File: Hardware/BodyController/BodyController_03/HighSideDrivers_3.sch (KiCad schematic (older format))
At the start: 48 parts, among them U12 BTS50202EKAXUMA2, U13 BTS50202EKAXUMA2, U14 BTS50202EKAXUMA2, U15 BTS716G, U23 tps25940-q1

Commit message: started serious layout
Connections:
- net GND: now also U15.6 (GND3/4)
- net ECU_1_ISENSE renamed ECU_1_ISENSE_AI
- net ECU_2_ISENSE renamed ECU_2_ISENSE_AI
- net IC_CONTROLLER_ISENSE renamed IC_CONTROLLER_ISENSE_AI
- net LOCK_ISENSE renamed LOCK_ISENSE_AI
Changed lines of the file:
@@
 EESchema Schematic File Version 2
-LIBS:BodyController_03-rescue
 LIBS:power
 LIBS:device
@@
 LIBS:contrib
 LIBS:valves
+LIBS:HSD
+LIBS:micros
+LIBS:ICs
+LIBS:Connectors
 LIBS:BodyController_03-cache
 EELAYER 25 0
@@
 $Descr A4 11693 8268
 encoding utf-8
-Sheet 7 11
+Sheet 7 12
 Title ""
 Date ""
@@
 $EndComp
 $Comp
-L GND #PWR098
+L GND #PWR080
 U 1 1 5991C550
 P 2900 7050
-F 0 "#PWR098" H 2900 6800 50  0001 C CNN
+F 0 "#PWR080" H 2900 6800 50  0001 C CNN
 F 1 "GND" H 2900 6900 50  0000 C CNN
 F 2 "" H 2900 7050 50  0001 C CNN
@@
 $EndComp
 $Comp
-L GND #PWR099
+L GND #PWR081
 U 1 1 5991C557
 P 2600 6850
-F 0 "#PWR099" H 2600 6600 50  0001 C CNN
+F 0 "#PWR081" H 2600 6600 50  0001 C CNN
 F 1 "GND" H 2600 6700 50  0000 C CNN
 F 2 "" H 2600 6850 50  0001 C CNN
@@
 $EndComp
 $Comp
-L GND #PWR0100
+L GND #PWR082
 U 1 1 5991C559
 P 2050 6850
-F 0 "#PWR0100" H 2050 6600 50  0001 C CNN
+F 0 "#PWR082" H 2050 6600 50  0001 C CNN
 F 1 "GND" H 2050 6700 50  0000 C CNN
 F 2 "" H 2050 6850 50  0001 C CNN
@@
 $EndComp
 $Comp
-L +12V #PWR0101
+L +12V #PWR083
 U 1 1 5991C55A
 P 4700 5600
-F 0 "#PWR0101" H 4700 5450 50  0001 C CNN
+F 0 "#PWR083" H 4700 5450 50  0001 C CNN
 F 1 "+12V" H 4700 5740 50  0000 C CNN
 F 2 "" H 4700 5600 50  0001 C CNN
@@
 $EndComp
 $Comp
-L +12V #PWR0102
+L +12V #PWR084
 U 1 1 5991C55C
 P 7600 750
-F 0 "#PWR0102" H 7600 600 50  0001 C CNN
+F 0 "#PWR084" H 7600 600 50  0001 C CNN
 F 1 "+12V" H 7600 890 50  0000 C CNN
 F 2 "" H 7600 750 50  0001 C CNN
@@
 $EndComp
 $Comp
-L GND #PWR0103
+L GND #PWR085
 U 1 1 5991C55D
 P 7600 2200
-F 0 "#PWR0103" H 7600 1950 50  0001 C CNN
+F 0 "#PWR085" H 7600 1950 50  0001 C CNN
 F 1 "GND" H 7600 2050 50  0000 C CNN
 F 2 "" H 7600 2200 50  0001 C CNN
@@
 $EndComp
 $Comp
-L GND #PWR0104
+L GND #PWR086
 U 1 1 5991C565
 P 2900 4900
-F 0 "#PWR0104" H 2900 4650 50  0001 C CNN
+F 0 "#PWR086" H 2900 4650 50  0001 C CNN
 F 1 "GND" H 2900 4750 50  0000 C CNN
 F 2 "" H 2900 4900 50  0001 C CNN
@@
 $EndComp
 $Comp
-L GND #PWR0105
+L GND #PWR087
 U 1 1 5991C56C
 P 2600 4700
-F 0 "#PWR0105" H 2600 4450 50  0001 C CNN
+F 0 "#PWR087" H 2600 4450 50  0001 C CNN
 F 1 "GND" H 2600 4550 50  0000 C CNN
 F 2 "" H 2600 4700 50  0001 C CNN
@@
 $EndComp
 $Comp
-L GND #PWR0106
+L GND #PWR088
 U 1 1 5991C56E
 P 2050 4700
-F 0 "#PWR0106" H 2050 4450 50  0001 C CNN
+F 0 "#PWR088" H 2050 4450 50  0001 C CNN
 F 1 "GND" H 2050 4550 50  0000 C CNN
 F 2 "" H 2050 4700 50  0001 C CNN
@@
 $EndComp
 $Comp
-L +12V #PWR0107
+L +12V #PWR089
 U 1 1 5991C56F
 P 4700 3450
-F 0 "#PWR0107" H 4700 3300 50  0001 C CNN
+F 0 "#PWR089" H 4700 3300 50  0001 C CNN
 F 1 "+12V" H 4700 3590 50  0000 C CNN
 F 2 "" H 4700 3450 50  0001 C CNN
@@
 $EndComp
 $Comp
-L GND #PWR0108
+L GND #PWR090
 U 1 1 5991C571
 P 2900 2900
-F 0 "#PWR0108" H 2900 2650 50  0001 C CNN
+F 0 "#PWR090" H 2900 2650 50  0001 C CNN
 F 1 "GND" H 2900 2750 50  0000 C CNN
 F 2 "" H 2900 2900 50  0001 C CNN
@@
 $EndComp
 $Comp
-L GND #PWR0109
+L GND #PWR091
 U 1 1 5991C578
 P 2600 2700
-F 0 "#PWR0109" H 2600 2450 50  0001 C CNN
+F 0 "#PWR091" H 2600 2450 50  0001 C CNN
 F 1 "GND" H 2600 2550 50  0000 C CNN
 F 2 "" H 2600 2700 50  0001 C CNN
@@
 $EndComp
 $Comp
-L GND #PWR0110
+L GND #PWR092
 U 1 1 5991C57A
 P 2050 2700
-F 0 "#PWR0110" H 2050 2450 50  0001 C CNN
+F 0 "#PWR092" H 2050 2450 50  0001 C CNN
 F 1 "GND" H 2050 2550 50  0000 C CNN
 F 2 "" H 2050 2700 50  0001 C CNN
@@
 $EndComp
 $Comp
-L +12V #PWR0111
+L +12V #PWR093
 U 1 1 5991C57B
 P 4700 1450
-F 0 "#PWR0111" H 4700 1300 50  0001 C CNN
+F 0 "#PWR093" H 4700 1300 50  0001 C CNN
 F 1 "+12V" H 4700 1590 50  0000 C CNN
 F 2 "" H 4700 1450 50  0001 C CNN
@@
 $EndComp
 $Comp
-L GND #PWR0112
+L GND #PWR094
 U 1 1 5991EDF3
 P 4500 7150
-F 0 "#PWR0112" H 4500 6900 50  0001 C CNN
+F 0 "#PWR094" H 4500 6900 50  0001 C CNN
 F 1 "GND" H 4500 7000 50  0000 C CNN
 F 2 "" H 4500 7150 50  0001 C CNN
@@
 $EndComp
 $Comp
-L GND #PWR0113
+L GND #PWR095
 U 1 1 5991EE88
 P 4750 7150
-F 0 "#PWR0113" H 4750 6900 50  0001 C CNN
+F 0 "#PWR095" H 4750 6900 50  0001 C CNN
 F 1 "GND" H 4750 7000 50  0000 C CNN
 F 2 "" H 4750 7150 50  0001 C CNN
@@
 $EndComp
 $Comp
-L GND #PWR0114
+L GND #PWR096
 U 1 1 59923191
 P 8950 1950
-F 0 "#PWR0114" H 8950 1700 50  0001 C CNN
+F 0 "#PWR096" H 8950 1700 50  0001 C CNN
 F 1 "GND" H 8950 1800 50  0000 C CNN
 F 2 "" H 8950 1950 50  0001 C CNN
@@
 $EndComp
 $Comp
-L GND #PWR0115
+L GND #PWR097
 U 1 1 5992320B
 P 9200 1950
-F 0 "#PWR0115" H 9200 1700 50  0001 C CNN
+F 0 "#PWR097" H 9200 1700 50  0001 C CNN
 F 1 "GND" H 9200 1800 50  0000 C CNN
 F 2 "" H 9200 1950 50  0001 C CNN
@@
 $EndComp
 $Comp
-L GND #PWR0116
+L GND #PWR098
 U 1 1 59923324
 P 9450 1950
-F 0 "#PWR0116" H 9450 1700 50  0001 C CNN
+F 0 "#PWR098" H 9450 1700 50  0001 C CNN
 F 1 "GND" H 9450 1800 50  0000 C CNN
 F 2 "" H 9450 1950 50  0001 C CNN
@@
 $EndComp
 $Comp
-L GND #PWR0117
+L GND #PWR099
 U 1 1 5992339E
 P 9700 1950
-F 0 "#PWR0117" H 9700 1700 50  0001 C CNN
+F 0 "#PWR099" H 9700 1700 50  0001 C CNN
 F 1 "GND" H 9700 1800 50  0000 C CNN
 F 2 "" H 9700 1950 50  0001 C CNN
@@
 $EndComp
 $Comp
-L +12V #PWR0118
+L +12V #PWR0100
 U 1 1 59A07BF7
 P 6200 3250
-F 0 "#PWR0118" H 6200 3100 50  0001 C CNN
+F 0 "#PWR0100" H 6200 3100 50  0001 C CNN
 F 1 "+12V" H 6200 3390 50  0000 C CNN
 F 2 "" H 6200 3250 50  0001 C CNN
@@
 $EndComp
 $Comp
-L GND #PWR0119
+L GND #PWR0101
 U 1 1 59A0E18C
 P 6200 5050
-F 0 "#PWR0119" H 6200 4800 50  0001 C CNN
+F 0 "#PWR0101" H 6200 4800 50  0001 C CNN
 F 1 "GND" H 6200 4900 50  0000 C CNN
 F 2 "" H 6200 5050 50  0001 C CNN
@@
 $EndComp
 $Comp
-L GND #PWR0120
+L GND #PWR0102
 U 1 1 59A0EE0E
 P 8900 5200
-F 0 "#PWR0120" H 8900 4950 50  0001 C CNN
+F 0 "#PWR0102" H 8900 4950 50  0001 C CNN
 F 1 "GND" H 8900 5050 50  0000 C CNN
 F 2 "" H 8900 5200 50  0001 C CNN
@@
 $EndComp
 $Comp
-L GND #PWR0121
+L GND #PWR0103
 U 1 1 59A0F52A
 P 9450 5200
-F 0 "#PWR0121" H 9450 4950 50  0001 C CNN
+F 0 "#PWR0103" H 9450 4950 50  0001 C CNN
 F 1 "GND" H 9450 5050 50  0000 C CNN
 F 2 "" H 9450 5200 50  0001 C CNN
@@
 $EndComp
 $Comp
-L GND #PWR0122
+L GND #PWR0104
 U 1 1 59A0FCD2
 P 6400 5050
-F 0 "#PWR0122" H 6400 4800 50  0001 C CNN
+F 0 "#PWR0104" H 6400 4800 50  0001 C CNN
 F 1 "GND" H 6400 4900 50  0000 C CNN
 F 2 "" H 6400 5050 50  0001 C CNN
@@
 $EndComp
 $Comp
-L GND #PWR0123
+L GND #PWR0105
 U 1 1 59A0FD67
 P 6600 5050
-F 0 "#PWR0123" H 6600 4800 50  0001 C CNN
+F 0 "#PWR0105" H 6600 4800 50  0001 C CNN
 F 1 "GND" H 6600 4900 50  0000 C CNN
 F 2 "" H 6600 5050 50  0001 C CNN
@@
 $EndComp
 $Comp
-L GND #PWR0124
+L GND #PWR0106
 U 1 1 59A0FDFC
 P 6800 5050
-F 0 "#PWR0124" H 6800 4800 50  0001 C CNN
+F 0 "#PWR0106" H 6800 4800 50  0001 C CNN
 F 1 "GND" H 6800 4900 50  0000 C CNN
 F 2 "" H 6800 5050 50  0001 C CNN
@@
 $EndComp
 $Comp
-L +3V3 #PWR0125
+L +3V3 #PWR0107
 U 1 1 59A12907
 P 9100 4200
-F 0 "#PWR0125" H 9100 4050 50  0001 C CNN
+F 0 "#PWR0107" H 9100 4050 50  0001 C CNN
 F 1 "+3V3" H 9100 4340 50  0000 C CNN
 F 2 "" H 9100 4200 50  0001 C CNN
@@
 $EndComp
 $Comp
-L +3V3 #PWR0126
+L +3V3 #PWR0108
 U 1 1 59A1297B
 P 9350 4200
-F 0 "#PWR0126" H 9350 4050 50  0001 C CNN
+F 0 "#PWR0108" H 9350 4050 50  0001 C CNN
 F 1 "+3V3" H 9350 4340 50  0000 C CNN
 F 2 "" H 9350 4200 50  0001 C CNN
@@
 $EndComp
 $Comp
-L GND #PWR0127
+L GND #PWR0109
 U 1 1 59A17E07
 P 8850 4050
-F 0 "#PWR0127" H 8850 3800 50  0001 C CNN
+F 0 "#PWR0109" H 8850 3800 50  0001 C CNN
 F 1 "GND" H 8850 3900 50  0000 C CNN
 F 2 "" H 8850 4050 50  0001 C CNN
@@
 DIAG_EN
 Text GLabel 1950 6400 0    59   Output ~ 0
-LOCK_ISENSE
+LOCK_ISENSE_AI
 Text GLabel 4850 6200 2    59   Output ~ 0
 CHARGE_PORT_RELEASE_OUT
@@
 DIAG_EN
 Text GLabel 1950 4250 0    59   Output ~ 0
-ECU_2_ISENSE
+ECU_2_ISENSE_AI
 Text GLabel 4600 4050 2    59   Output ~ 0
 MOTOR_CONTROLLER_OUT
@@
 DIAG_SELECT
 Text GLabel 1950 2250 0    59   Output ~ 0
-ECU_1_ISENSE
+ECU_1_ISENSE_AI
 Text GLabel 4850 2050 2    59   Output ~ 0
 BMS_CONTROLLER_OUT
@@
 IC_CONTROLLER_~FLT
 Text GLabel 9650 4800 2    59   Output ~ 0
-IC_CONTROLLER_ISENSE
+IC_CONTROLLER_ISENSE_AI
 Text GLabel 4850 2500 2    59   Output ~ 0
 J1772_CONTROLLER_OUT
@@
 Connection ~ 8550 750
 NoConn ~ 8650 4200
+Connection ~ 7600 2050
 $EndSCHEMATC

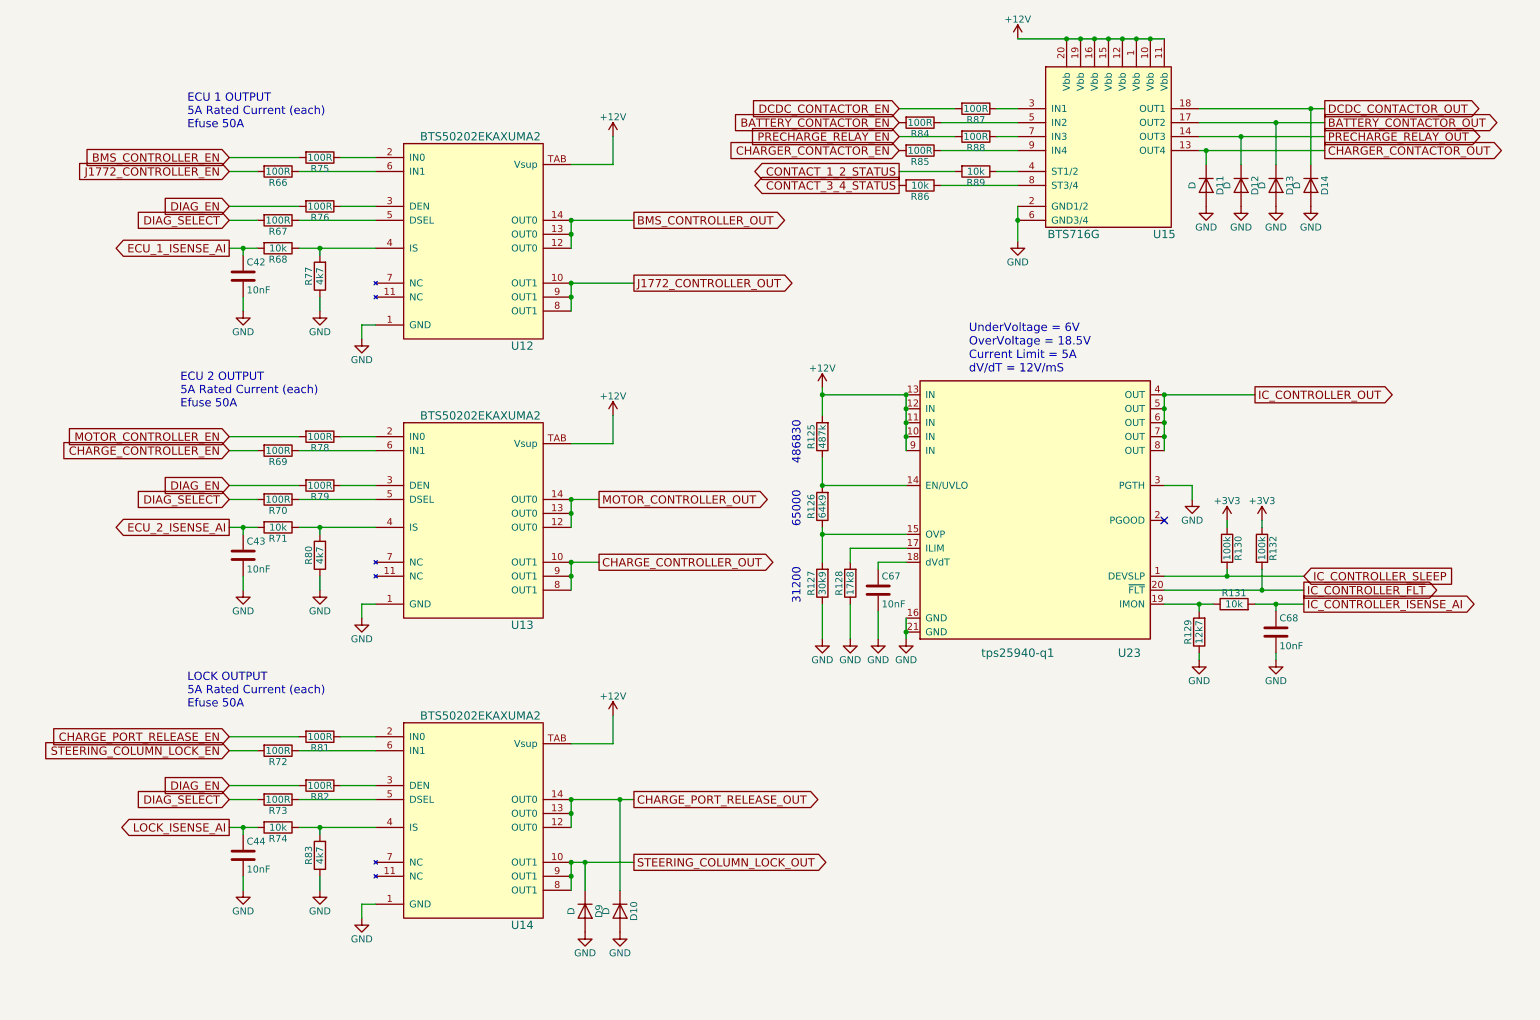
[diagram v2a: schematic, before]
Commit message: Body Controller Layout Done
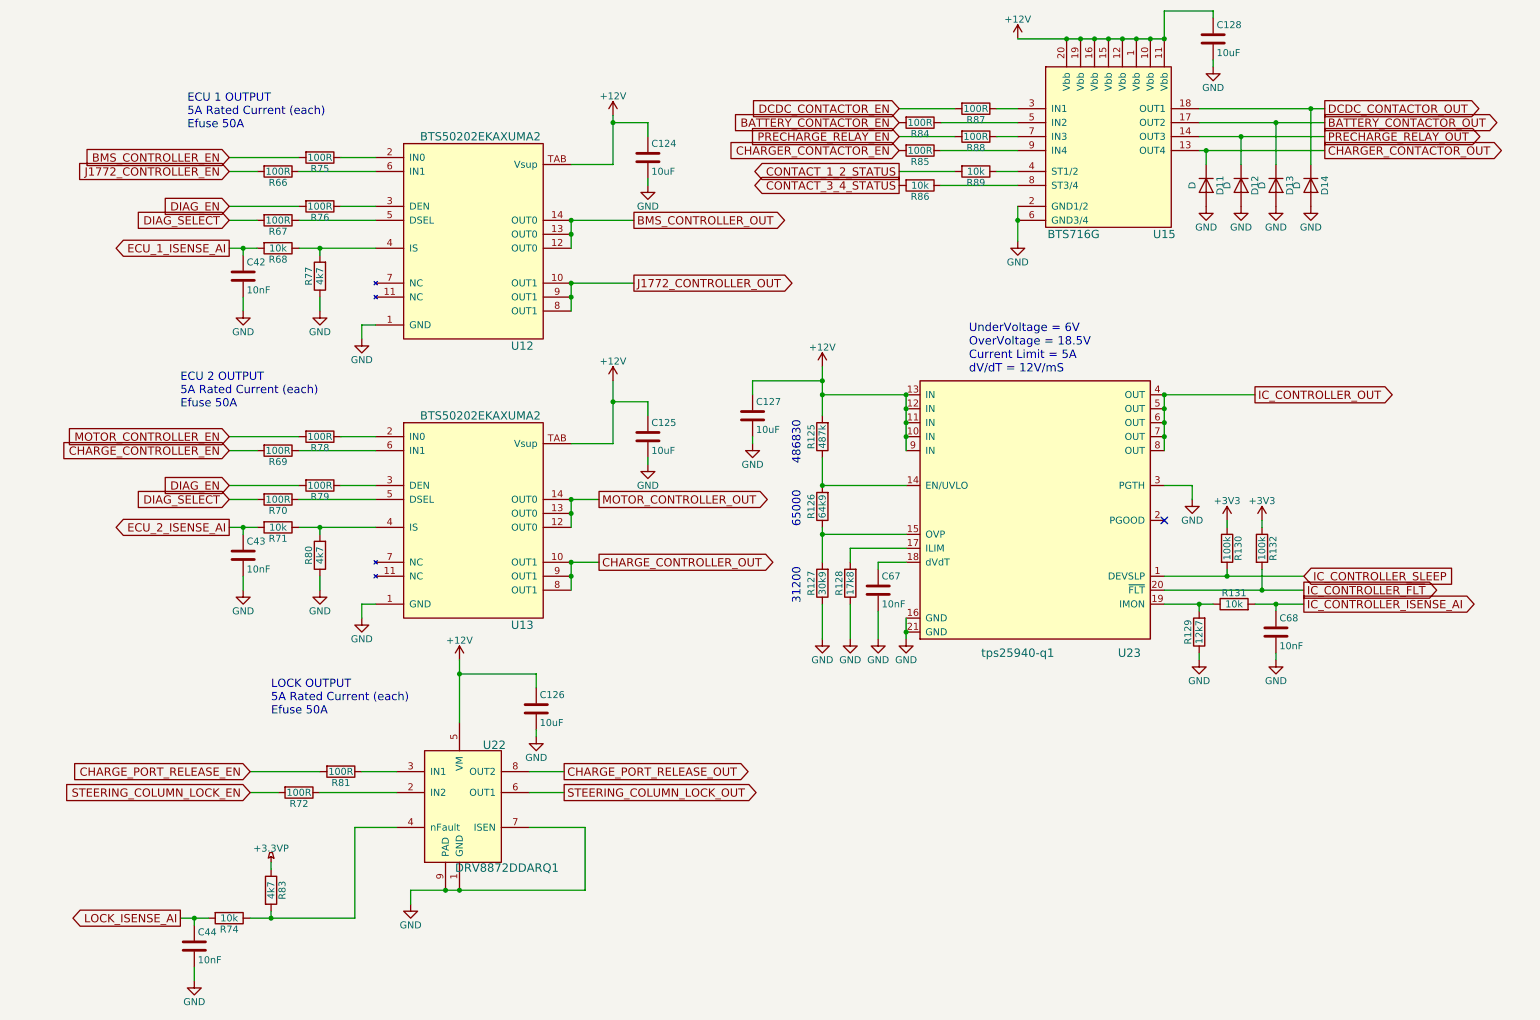
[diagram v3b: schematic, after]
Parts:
- removed D10, D9: D, Diodes_SMD:D_SMB, symbol D
- removed R73, R82: 100R, Resistors_SMD:R_0603, symbol R
- removed U14: BTS50202EKAXUMA2, Footprints:PG_DSO_14_40_EP, symbol BTS50202EKAXUMA2
- added C124, C125, C126, C127, C128: 10uF, Capacitors_SMD:C_1206, symbol C
- added U22: DRV8872DDARQ1, Housings_SOIC:HTSOP-8-1EP_3.9x4.9mm_Pitch1.27mm_ThermalVias, symbol DRV8872DDARQ1
- D11, D12, D13, D14: footprint Diodes_SMD:D_SMB -> Diodes_SMD:D_PowerDI-123; PartNumber S3AB -> DFLS1100Q-7
- U12, U13: PartNumber (none) -> BTS50202EKAXUMA2
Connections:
- net +12V: now also C124.1, C125.1, C126.1, C127.1, C128.1, U22.5 (VM)
- net CHARGE_PORT_RELEASE_OUT: now also U22.8 (OUT2)
- net GND: now also C124.2, C125.2, C126.2, C127.2, C128.2, U22.1 (GND), U22.7 (ISEN), U22.9 (PAD); no longer R83.1
- net STEERING_COLUMN_LOCK_OUT: now also U22.6 (OUT1)
- net at R81.1: now also U22.3 (IN1)
- net at R74.1, R83.2: now also U22.4 (nFault)
- net at R72.1: now also U22.2 (IN2)
- new net +3.3VP: R83.1
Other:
- moved on the sheet: C44, R72, R74, R81, R83

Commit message: Added resistor values via BOM importer. Changed layout file to add large CAN resistors and buffer to 1.65V Reference
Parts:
- R125: PartNumber (none) -> ERJ-3EKF4873V
- R126: PartNumber (none) -> ERJ-3EKF6492V
- R127: PartNumber (none) -> ERJ-3EKF3092V
- R128: PartNumber (none) -> RG1608P-3092-B-T5
- R129: PartNumber (none) -> AC0603FR-0712K7L
- R130, R132: PartNumber (none) -> AC0603FR-07100KL
- R131, R68, R71, R74, R86, R89: PartNumber (none) -> AC0603FR-0710KL
- R66, R67, R69, R70, R72, R75, R76, R78, R79, R81, R84, R85, R87, R88: PartNumber (none) -> AC0603FR-07100RL
- R77, R80, R83: PartNumber (none) -> AC0603FR-074K7L
